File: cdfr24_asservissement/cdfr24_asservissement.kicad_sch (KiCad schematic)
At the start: 59 parts, among them J1 Connecteur batterie, J10 Free Connecteur, J11 Conn_01x02, J12 Conn_01x02, J13 Connecteur Odométrie, J14 Conn_ST_STDC14, J2 Conn_01x03, J3 Conn_01x05, J4 Connecteur Programmation, J5 Conn_01x03, J6 Connecteur Odométrie, J7 Conn_01x03, Q13 Q_NMOS_GDS, U1 LM317_SOT-223, U3 STM32F401RCTx, U4 LMR16020PDDA, U4 LSM6DSL, Y1 Crystal_GND24

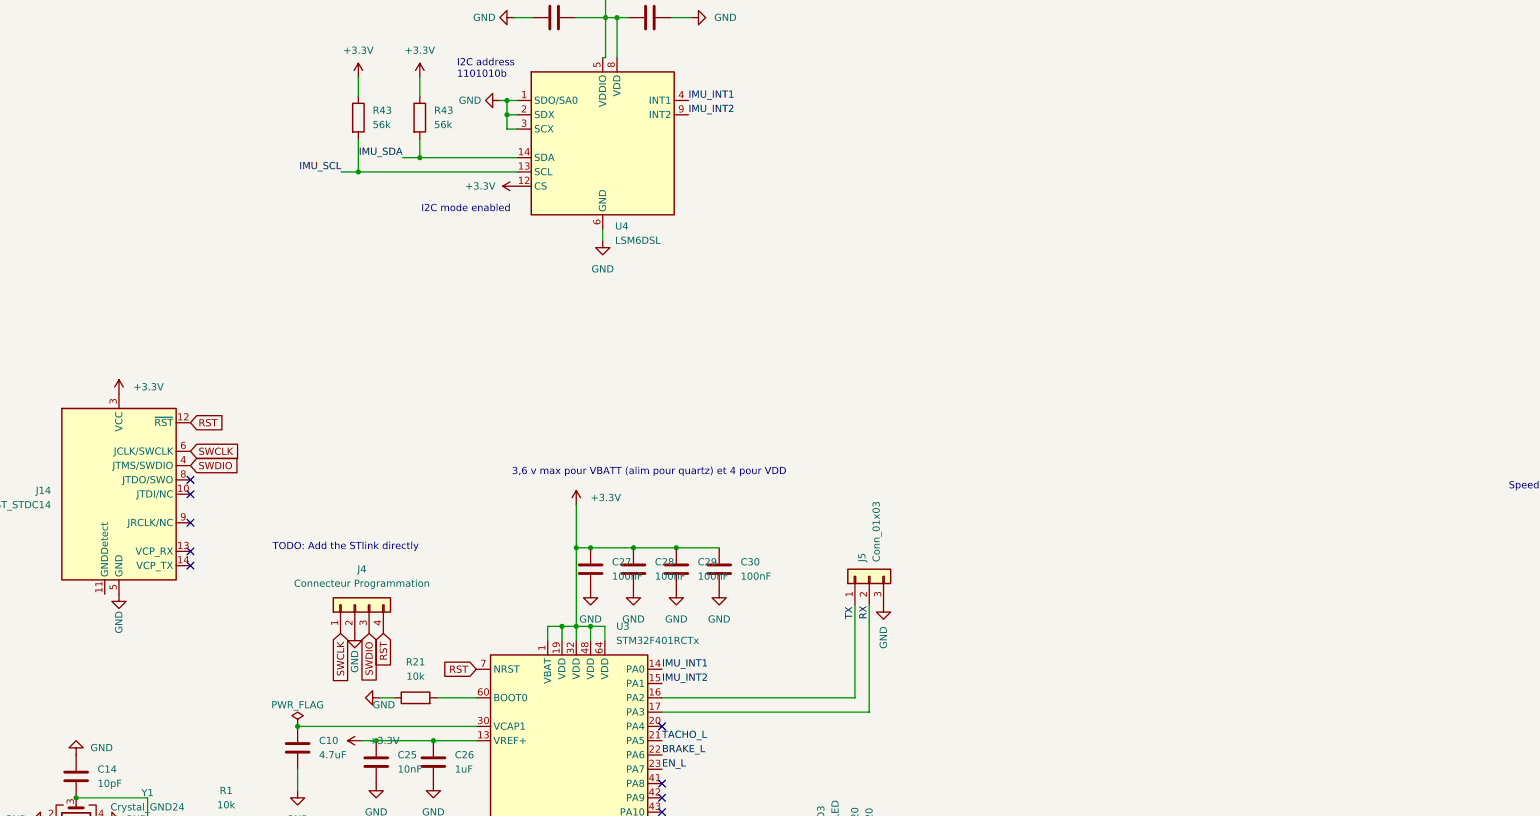
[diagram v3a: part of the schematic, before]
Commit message: Add footprints
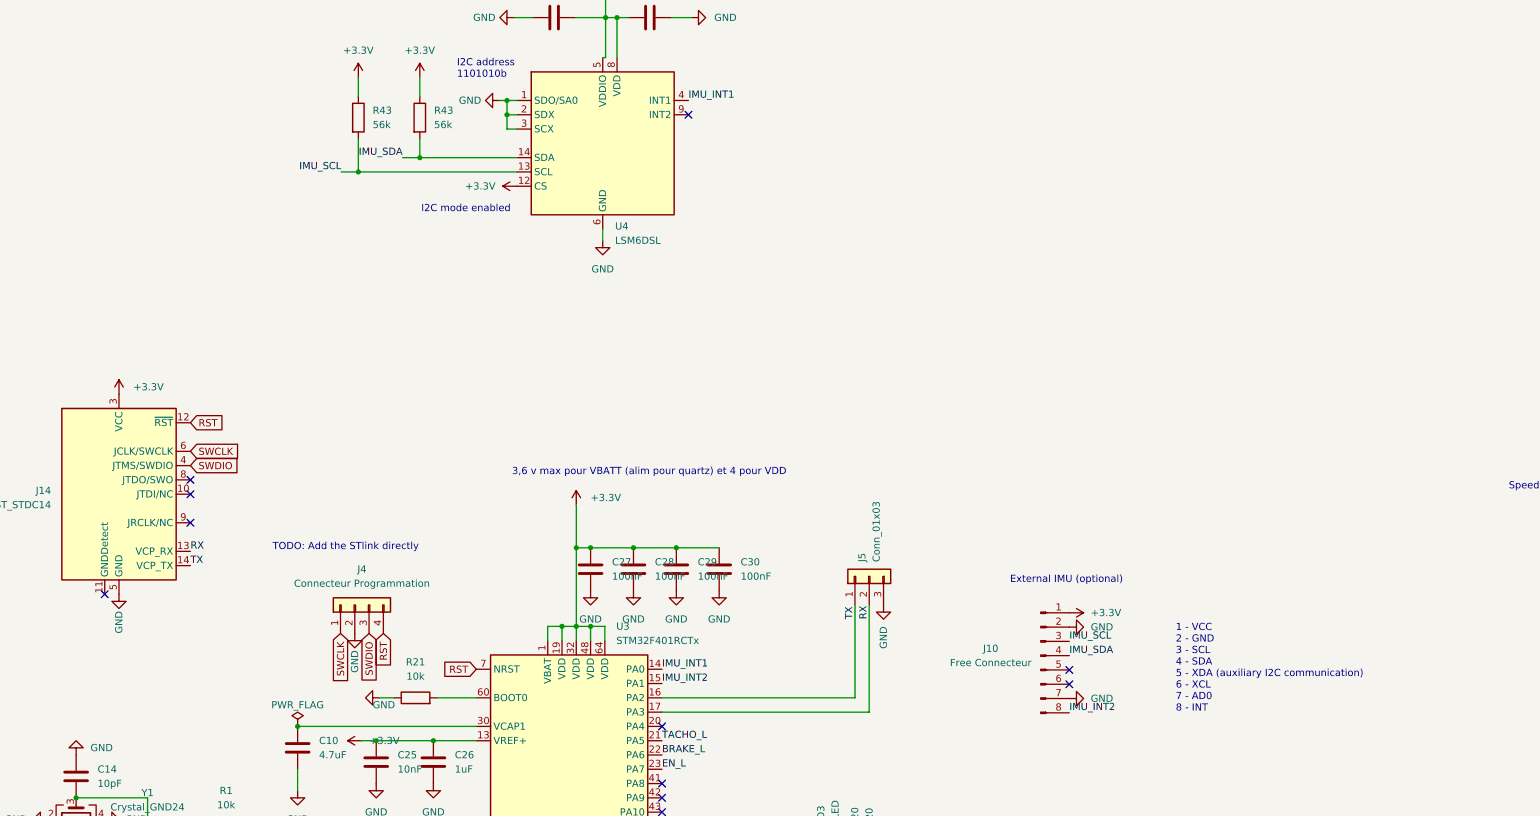
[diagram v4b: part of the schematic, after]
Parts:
- added J10: Free Connecteur, Connector_PinHeader_2.54mm:PinHeader_1x08_P2.54mm_Vertical, symbol Connector:Conn_01x08_Male
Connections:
- net +3.3V: now also J10.1 (Pin_1)
- net GND: now also J10.2 (Pin_2), J10.7 (Pin_7)
- net IMU_INT2: now also J10.8 (Pin_8); no longer U4.9 (INT2)
- net IMU_SCL: now also J10.3 (Pin_3)
- net IMU_SDA: now also J10.4 (Pin_4)
- net RX: now also J14.13 (VCP_RX)
- net TX: now also J14.14 (VCP_TX)
- no-connect marks 20 -> 22
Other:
- note added: "1 - VCC 2 - GND 3 - SCL 4 - SDA 5 - XDA (auxiliary I2C communication) 6 - XCL 7 - AD0 8 - INT"
- note added: "External IMU (optional)"
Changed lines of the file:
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@@
   (junction (at 145.415 236.22) (diameter 0) (color 0 0 0 0)
   )
-  (no_connect (at 79.375 225.425))
+  (no_connect (at 235.585 243.967))
+  (no_connect (at 167.894 145.288))
   (no_connect (at 79.375 212.725))
   (no_connect (at 163.195 320.04))
@@
   (no_connect (at 130.175 309.88))
   (no_connect (at 79.375 210.185))
+  (no_connect (at 235.585 246.507))
   (no_connect (at 83.185 53.975))
   (no_connect (at 163.195 314.96))
@@
   (no_connect (at 163.195 269.24))
   (no_connect (at 130.175 279.4))
-  (no_connect (at 79.375 222.885))
   (no_connect (at 163.195 254))
   (no_connect (at 79.375 217.805))
   (no_connect (at 163.195 264.16))
   (no_connect (at 163.195 307.34))
+  (no_connect (at 64.135 230.505))
   (no_connect (at 163.195 266.7))
   (wire (pts (xy 335.026 218.44) (xy 345.567 218.44))
@@
     (effects (font (size 4 4)) (justify left bottom))
   )
+  (text "1 - VCC\n2 - GND\n3 - SCL\n4 - SDA\n5 - XDA (auxiliary I2C communication)\n6 - XCL\n7 - AD0\n8 - INT"
+    (at 254.508 251.587 0)
+    (effects (font (size 1.27 1.27)) (justify left bottom))
+  )
   (text "Speed control pin" (at 313.69 212.09 0)
     (effects (font (size 1.27 1.27)) (justify left bottom))
@@
     (effects (font (size 1.27 1.27)) (justify left bottom))
   )
+  (text "External IMU (optional)" (at 225.044 228.727 0)
+    (effects (font (size 1.27 1.27)) (justify left bottom))
+  )
   (text "I2C address\n1101010b" (at 126.746 138.938 0)
     (effects (font (size 1.27 1.27)) (justify left bottom))
@@
     (effects (font (size 1.27 1.27)) (justify left bottom))
   )
+  (label "IMU_INT2" (at 235.585 251.587 0) (fields_autoplaced)
+    (effects (font (size 1.27 1.27)) (justify left bottom))
+  )
   (label "IMU_INT2" (at 163.195 246.38 0) (fields_autoplaced)
     (effects (font (size 1.27 1.27)) (justify left bottom))
@@
     (effects (font (size 1.27 1.27)) (justify left bottom))
   )
-  (label "IMU_INT2" (at 167.894 145.288 0) (fields_autoplaced)
+  (label "TX" (at 79.375 225.425 0) (fields_autoplaced)
     (effects (font (size 1.27 1.27)) (justify left bottom))
   )
@@
     (effects (font (size 1.27 1.27)) (justify left bottom))
   )
+  (label "IMU_SDA" (at 235.585 241.427 0) (fields_autoplaced)
+    (effects (font (size 1.27 1.27)) (justify left bottom))
+  )
   (label "TACHO_R" (at 130.175 299.72 180) (fields_autoplaced)
     (effects (font (size 1.27 1.27)) (justify right bottom))
@@
     (effects (font (size 1.27 1.27)) (justify left bottom))
   )
+  (label "RX" (at 79.375 222.885 0) (fields_autoplaced)
+    (effects (font (size 1.27 1.27)) (justify left bottom))
+  )
+  (label "IMU_SCL" (at 235.585 238.887 0) (fields_autoplaced)
+    (effects (font (size 1.27 1.27)) (justify left bottom))
+  )
   (label "BRAKE_L" (at 335.026 115.824 0) (fields_autoplaced)
     (effects (font (size 1.27 1.27)) (justify left bottom))
@@
     )
   )
+  (symbol (lib_id "power:+3.3V") (at 235.585 233.807 270) (unit 1)
+    (in_bom yes) (on_board yes) (dnp no) (fields_autoplaced)
+    (property "Reference" "#PWR05" (at 231.775 233.807 0)
+      (effects (font (size 1.27 1.27)) hide)
+    )
+    (property "Value" "+3.3V" (at 239.395 233.8069 90)
+      (effects (font (size 1.27 1.27)) (justify left))
+    )
+    (property "Footprint" "" (at 235.585 233.807 0)
+      (effects (font (size 1.27 1.27)) hide)
+    )
+    (property "Datasheet" "" (at 235.585 233.807 0)
+      (effects (font (size 1.27 1.27)) hide)
+    )
+    (pin "1")
+    (instances
+      (project "Asservissement_CDFR_2023"
+        (path "/aba37299-4f54-471d-ab35-d760532fd54c"
+          (reference "#PWR05") (unit 1)
+        )
+      )
+      (project "cdfr24_asservissement"
+        (path "/c6b82269-16f5-49e6-8b51-4d12a40a3077"
+          (reference "#PWR056") (unit 1)
+        )
+      )
+    )
+  )
   (symbol (lib_id "Device:C_Polarized") (at 71.755 40.005 0) (unit 1)
     (in_bom yes) (on_board yes) (dnp no) (fields_autoplaced)
@@
     )
   )
+  (symbol (lib_id "power:GND") (at 235.585 236.347 90) (unit 1)
+    (in_bom yes) (on_board yes) (dnp no) (fields_autoplaced)
+    (property "Reference" "#PWR09" (at 241.935 236.347 0)
+      (effects (font (size 1.27 1.27)) hide)
+    )
+    (property "Value" "GND" (at 239.395 236.347 90)
+      (effects (font (size 1.27 1.27)) (justify right))
+    )
+    (property "Footprint" "" (at 235.585 236.347 0)
+      (effects (font (size 1.27 1.27)) hide)
+    )
+    (property "Datasheet" "" (at 235.585 236.347 0)
+      (effects (font (size 1.27 1.27)) hide)
+    )
+    (pin "1")
+    (instances
+      (project "Asservissement_CDFR_2023"
+        (path "/aba37299-4f54-471d-ab35-d760532fd54c"
+          (reference "#PWR09") (unit 1)
+        )
+      )
+      (project "cdfr24_asservissement"
+        (path "/c6b82269-16f5-49e6-8b51-4d12a40a3077"
+          (reference "#PWR073") (unit 1)
+        )
+      )
+    )
+  )
   (symbol (lib_id "power:+3.3V") (at 271.145 38.735 270) (unit 1)
     (in_bom yes) (on_board yes) (dnp no) (fields_autoplaced)
@@
     )
   )
+  (symbol (lib_id "Connector:Conn_01x08_Male") (at 230.505 241.427 0) (unit 1)
+    (in_bom yes) (on_board yes) (dnp no)
+    (property "Reference" "J10" (at 221.615 240.157 0)
+      (effects (font (size 1.27 1.27)))
+    )
+    (property "Value" "Free Connecteur" (at 221.615 242.697 0)
+      (effects (font (size 1.27 1.27)))
+    )
+    (property "Footprint" "Connector_PinHeader_2.54mm:PinHeader_1x08_P2.54mm_Vertical" (at 230.505 241.427 0)
+      (effects (font (size 1.27 1.27)) hide)
+    )
+    (property "Datasheet" "~" (at 230.505 241.427 0)
+      (effects (font (size 1.27 1.27)) hide)
+    )
+    (pin "1")
+    (pin "2")
+    (pin "3")
+    (pin "4")
+    (pin "5")
+    (pin "6")
+    (pin "7")
+    (pin "8")
+    (instances
+      (project "Asservissement_CDFR_2023"
+        (path "/aba37299-4f54-471d-ab35-d760532fd54c"
+          (reference "J10") (unit 1)
+        )
+      )
+      (project "cdfr24_asservissement"
+        (path "/c6b82269-16f5-49e6-8b51-4d12a40a3077"
+          (reference "J15") (unit 1)
+        )
+      )
+    )
+  )
   (symbol (lib_id "power:GND") (at 64.135 270.51 90) (unit 1)
     (in_bom yes) (on_board yes) (dnp no)
@@
         )
       )
+    )
+  )
+  (symbol (lib_id "power:GND") (at 235.585 249.047 90) (unit 1)
+    (in_bom yes) (on_board yes) (dnp no) (fields_autoplaced)
+    (property "Reference" "#PWR09" (at 241.935 249.047 0)
+      (effects (font (size 1.27 1.27)) hide)
+    )
+    (property "Value" "GND" (at 239.395 249.047 90)
+      (effects (font (size 1.27 1.27)) (justify right))
+    )
+    (property "Footprint" "" (at 235.585 249.047 0)
+      (effects (font (size 1.27 1.27)) hide)
+    )
+    (property "Datasheet" "" (at 235.585 249.047 0)
+      (effects (font (size 1.27 1.27)) hide)
+    )
+    (pin "1")
+    (instances
+      (project "Asservissement_CDFR_2023"
+        (path "/aba37299-4f54-471d-ab35-d760532fd54c"
+          (reference "#PWR09") (unit 1)
+        )
+      )
+      (project "cdfr24_asservissement"
+        (path "/c6b82269-16f5-49e6-8b51-4d12a40a3077"
+          (reference "#PWR074") (unit 1)
+        )
+      )

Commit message: Resolve some errors
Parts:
- added H1, H2, H3, H4: MountingHole_Pad, MountingHole:MountingHole_3.2mm_M3_Pad_Via, symbol Mechanical:MountingHole_Pad
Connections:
- net GND: now also H1.1, H2.1, H3.1, H4.1
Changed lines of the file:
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@@
+    )
+  )
+  (symbol (lib_id "power:GND") (at 45.72 391.16 0) (unit 1)
+    (in_bom yes) (on_board yes) (dnp no) (fields_autoplaced)
+    (property "Reference" "#PWR078" (at 45.72 397.51 0)
+      (effects (font (size 1.27 1.27)) hide)
+    )
+    (property "Value" "GND" (at 45.72 396.24 0)
+      (effects (font (size 1.27 1.27)))
+    )
+    (property "Footprint" "" (at 45.72 391.16 0)
+      (effects (font (size 1.27 1.27)) hide)
+    )
+    (property "Datasheet" "" (at 45.72 391.16 0)
+      (effects (font (size 1.27 1.27)) hide)
+    )
+    (pin "1")
+    (instances
+      (project "Asservissement_CDFR_2023"
+        (path "/aba37299-4f54-471d-ab35-d760532fd54c"
+          (reference "#PWR078") (unit 1)
+        )
+      )
+      (project "cdfr24_asservissement"
+        (path "/c6b82269-16f5-49e6-8b51-4d12a40a3077"
+          (reference "#PWR077") (unit 1)
+        )
+      )
     )
   )
@@
     )
   )
+  (symbol (lib_id "power:GND") (at 55.88 391.16 0) (unit 1)
+    (in_bom yes) (on_board yes) (dnp no) (fields_autoplaced)
+    (property "Reference" "#PWR079" (at 55.88 397.51 0)
+      (effects (font (size 1.27 1.27)) hide)
+    )
+    (property "Value" "GND" (at 55.88 396.24 0)
+      (effects (font (size 1.27 1.27)))
+    )
+    (property "Footprint" "" (at 55.88 391.16 0)
+      (effects (font (size 1.27 1.27)) hide)
+    )
+    (property "Datasheet" "" (at 55.88 391.16 0)
+      (effects (font (size 1.27 1.27)) hide)
+    )
+    (pin "1")
+    (instances
+      (project "Asservissement_CDFR_2023"
+        (path "/aba37299-4f54-471d-ab35-d760532fd54c"
+          (reference "#PWR079") (unit 1)
+        )
+      )
+      (project "cdfr24_asservissement"
+        (path "/c6b82269-16f5-49e6-8b51-4d12a40a3077"
+          (reference "#PWR078") (unit 1)
+        )
+      )
+    )
+  )
   (symbol (lib_id "Regulator_Linear:LM317_SOT-223") (at 219.075 38.735 0) (unit 1)
     (in_bom yes) (on_board yes) (dnp no) (fields_autoplaced)
@@
         (path "/c6b82269-16f5-49e6-8b51-4d12a40a3077"
           (reference "C11") (unit 1)
+        )
+      )
+    )
+  )
+  (symbol (lib_id "Mechanical:MountingHole_Pad") (at 29.21 388.62 0) (unit 1)
+    (in_bom yes) (on_board yes) (dnp no) (fields_autoplaced)
+    (property "Reference" "H1" (at 31.75 386.0799 0)
+      (effects (font (size 1.27 1.27)) (justify left))
+    )
+    (property "Value" "MountingHole_Pad" (at 31.75 388.6199 0)
+      (effects (font (size 1.27 1.27)) (justify left))
+    )
+    (property "Footprint" "MountingHole:MountingHole_3.2mm_M3_Pad_Via" (at 29.21 388.62 0)
+      (effects (font (size 1.27 1.27)) hide)
+    )
+    (property "Datasheet" "~" (at 29.21 388.62 0)
+      (effects (font (size 1.27 1.27)) hide)
+    )
+    (pin "1")
+    (instances
+      (project "Asservissement_CDFR_2023"
+        (path "/aba37299-4f54-471d-ab35-d760532fd54c"
+          (reference "H1") (unit 1)
+        )
+      )
+      (project "cdfr24_asservissement"
+        (path "/c6b82269-16f5-49e6-8b51-4d12a40a3077"
+          (reference "H1") (unit 1)
         )
       )
@@
     )
   )
+  (symbol (lib_id "Mechanical:MountingHole_Pad") (at 39.37 388.62 0) (unit 1)
+    (in_bom yes) (on_board yes) (dnp no) (fields_autoplaced)
+    (property "Reference" "H2" (at 41.91 386.0799 0)
+      (effects (font (size 1.27 1.27)) (justify left))
+    )
+    (property "Value" "MountingHole_Pad" (at 41.91 388.6199 0)
+      (effects (font (size 1.27 1.27)) (justify left))
+    )
+    (property "Footprint" "MountingHole:MountingHole_3.2mm_M3_Pad_Via" (at 39.37 388.62 0)
+      (effects (font (size 1.27 1.27)) hide)
+    )
+    (property "Datasheet" "~" (at 39.37 388.62 0)
+      (effects (font (size 1.27 1.27)) hide)
+    )
+    (pin "1")
+    (instances
+      (project "Asservissement_CDFR_2023"
+        (path "/aba37299-4f54-471d-ab35-d760532fd54c"
+          (reference "H2") (unit 1)
+        )
+      )
+      (project "cdfr24_asservissement"
+        (path "/c6b82269-16f5-49e6-8b51-4d12a40a3077"
+          (reference "H2") (unit 1)
+        )
+      )
+    )
+  )
   (symbol (lib_id "Connector_Generic:Conn_01x02") (at 71.755 331.47 90) (mirror x) (unit 1)
     (in_bom yes) (on_board yes) (dnp no) (fields_autoplaced)
@@
     )
   )
+  (symbol (lib_id "Mechanical:MountingHole_Pad") (at 45.72 388.62 0) (unit 1)
+    (in_bom yes) (on_board yes) (dnp no) (fields_autoplaced)
+    (property "Reference" "H3" (at 48.26 386.0799 0)
+      (effects (font (size 1.27 1.27)) (justify left))
+    )
+    (property "Value" "MountingHole_Pad" (at 48.26 388.6199 0)
+      (effects (font (size 1.27 1.27)) (justify left) hide)
+    )
+    (property "Footprint" "MountingHole:MountingHole_3.2mm_M3_Pad_Via" (at 45.72 388.62 0)
+      (effects (font (size 1.27 1.27)) hide)
+    )
+    (property "Datasheet" "~" (at 45.72 388.62 0)
+      (effects (font (size 1.27 1.27)) hide)
+    )
+    (pin "1")
+    (instances
+      (project "Asservissement_CDFR_2023"
+        (path "/aba37299-4f54-471d-ab35-d760532fd54c"
+          (reference "H3") (unit 1)
+        )
+      )
+      (project "cdfr24_asservissement"
+        (path "/c6b82269-16f5-49e6-8b51-4d12a40a3077"
+          (reference "H3") (unit 1)
+        )
+      )
+    )
+  )
   (symbol (lib_id "Connector_Generic:Conn_01x05") (at 398.526 75.438 270) (mirror x) (unit 1)
     (in_bom yes) (on_board yes) (dnp no) (fields_autoplaced)
@@
     )
   )
+  (symbol (lib_id "Mechanical:MountingHole_Pad") (at 55.88 388.62 0) (unit 1)
+    (in_bom yes) (on_board yes) (dnp no) (fields_autoplaced)
+    (property "Reference" "H4" (at 58.42 386.0799 0)
+      (effects (font (size 1.27 1.27)) (justify left))
+    )
+    (property "Value" "MountingHole_Pad" (at 58.42 388.6199 0)
+      (effects (font (size 1.27 1.27)) (justify left) hide)
+    )
+    (property "Footprint" "MountingHole:MountingHole_3.2mm_M3_Pad_Via" (at 55.88 388.62 0)
+      (effects (font (size 1.27 1.27)) hide)
+    )
+    (property "Datasheet" "~" (at 55.88 388.62 0)
+      (effects (font (size 1.27 1.27)) hide)
+    )
+    (pin "1")
+    (instances
+      (project "Asservissement_CDFR_2023"
+        (path "/aba37299-4f54-471d-ab35-d760532fd54c"
+          (reference "H4") (unit 1)
+        )
+      )
+      (project "cdfr24_asservissement"
+        (path "/c6b82269-16f5-49e6-8b51-4d12a40a3077"
+          (reference "H4") (unit 1)
+        )
+      )
+    )
+  )
   (symbol (lib_id "Device:R") (at 119.38 248.92 90) (unit 1)
     (in_bom yes) (on_board yes) (dnp no) (fields_autoplaced)
@@
     )
   )
+  (symbol (lib_id "power:GND") (at 39.37 391.16 0) (unit 1)
+    (in_bom yes) (on_board yes) (dnp no) (fields_autoplaced)
+    (property "Reference" "#PWR077" (at 39.37 397.51 0)
+      (effects (font (size 1.27 1.27)) hide)
+    )
+    (property "Value" "GND" (at 39.37 396.24 0)
+      (effects (font (size 1.27 1.27)))
+    )
+    (property "Footprint" "" (at 39.37 391.16 0)
+      (effects (font (size 1.27 1.27)) hide)
+    )
+    (property "Datasheet" "" (at 39.37 391.16 0)
+      (effects (font (size 1.27 1.27)) hide)
+    )
+    (pin "1")
+    (instances
+      (project "Asservissement_CDFR_2023"
+        (path "/aba37299-4f54-471d-ab35-d760532fd54c"
+          (reference "#PWR077") (unit 1)
+        )
+      )
+      (project "cdfr24_asservissement"
+        (path "/c6b82269-16f5-49e6-8b51-4d12a40a3077"
+          (reference "#PWR076") (unit 1)
+        )
+      )
+    )
+  )
   (symbol (lib_id "power:GND") (at 113.03 248.92 270) (unit 1)
     (in_bom yes) (on_board yes) (dnp no)
@@
         )
       )
+    )
+  )
+  (symbol (lib_id "power:GND") (at 29.21 391.16 0) (unit 1)
+    (in_bom yes) (on_board yes) (dnp no) (fields_autoplaced)
+    (property "Reference" "#PWR02" (at 29.21 397.51 0)
+      (effects (font (size 1.27 1.27)) hide)
+    )
+    (property "Value" "GND" (at 29.21 396.24 0)
+      (effects (font (size 1.27 1.27)))
+    )
+    (property "Footprint" "" (at 29.21 391.16 0)
+      (effects (font (size 1.27 1.27)) hide)
+    )
+    (property "Datasheet" "" (at 29.21 391.16 0)
+      (effects (font (size 1.27 1.27)) hide)
+    )
+    (pin "1")
+    (instances
+      (project "Asservissement_CDFR_2023"
+        (path "/aba37299-4f54-471d-ab35-d760532fd54c"
+          (reference "#PWR02") (unit 1)
+        )
+      )
+      (project "cdfr24_asservissement"
+        (path "/c6b82269-16f5-49e6-8b51-4d12a40a3077"
+          (reference "#PWR075") (unit 1)
+        )
+      )
